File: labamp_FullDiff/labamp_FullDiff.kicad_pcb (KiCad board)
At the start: 2 copper layers, 55 x 26 mm, 33 parts, among them J1 Conn_02x06_Odd_Even, J2 Conn_02x06_Odd_Even, J3 Conn_01x03, U3 THS4521ID

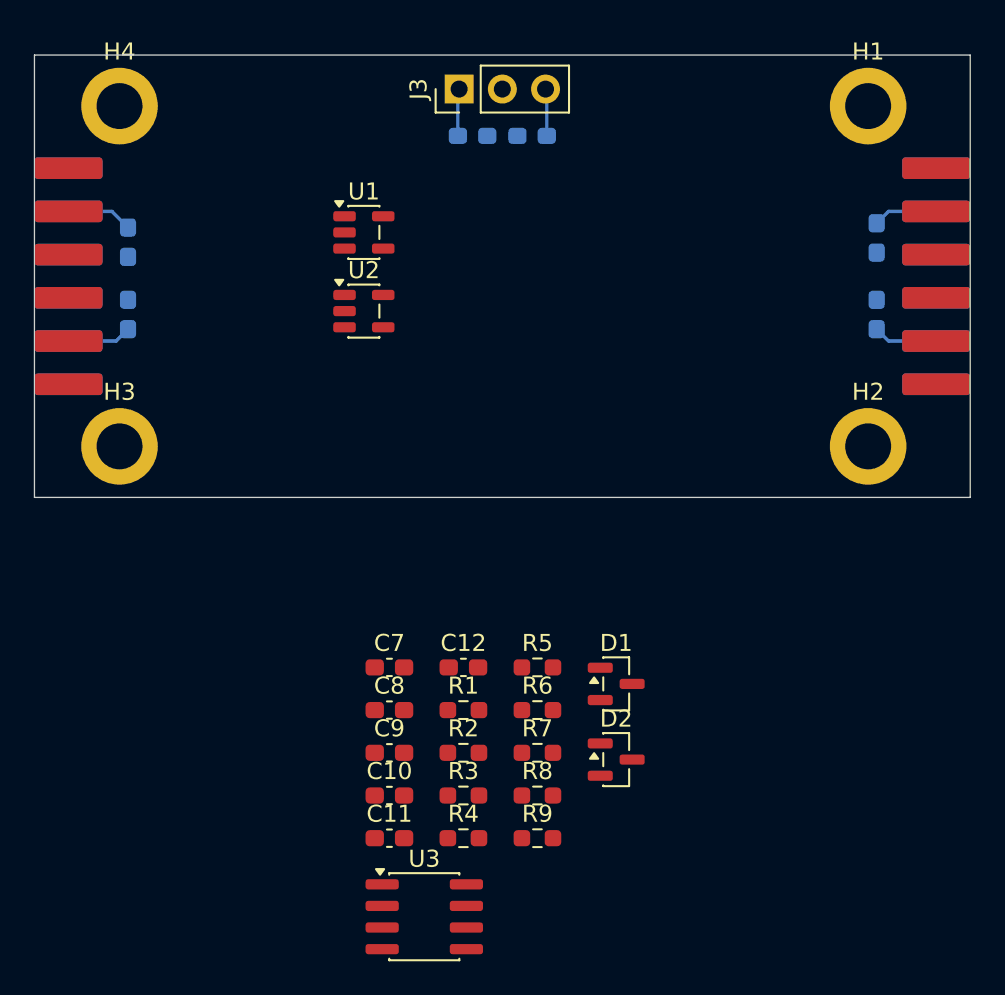
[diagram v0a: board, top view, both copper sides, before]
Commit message: PCB layout od Diff ampl started
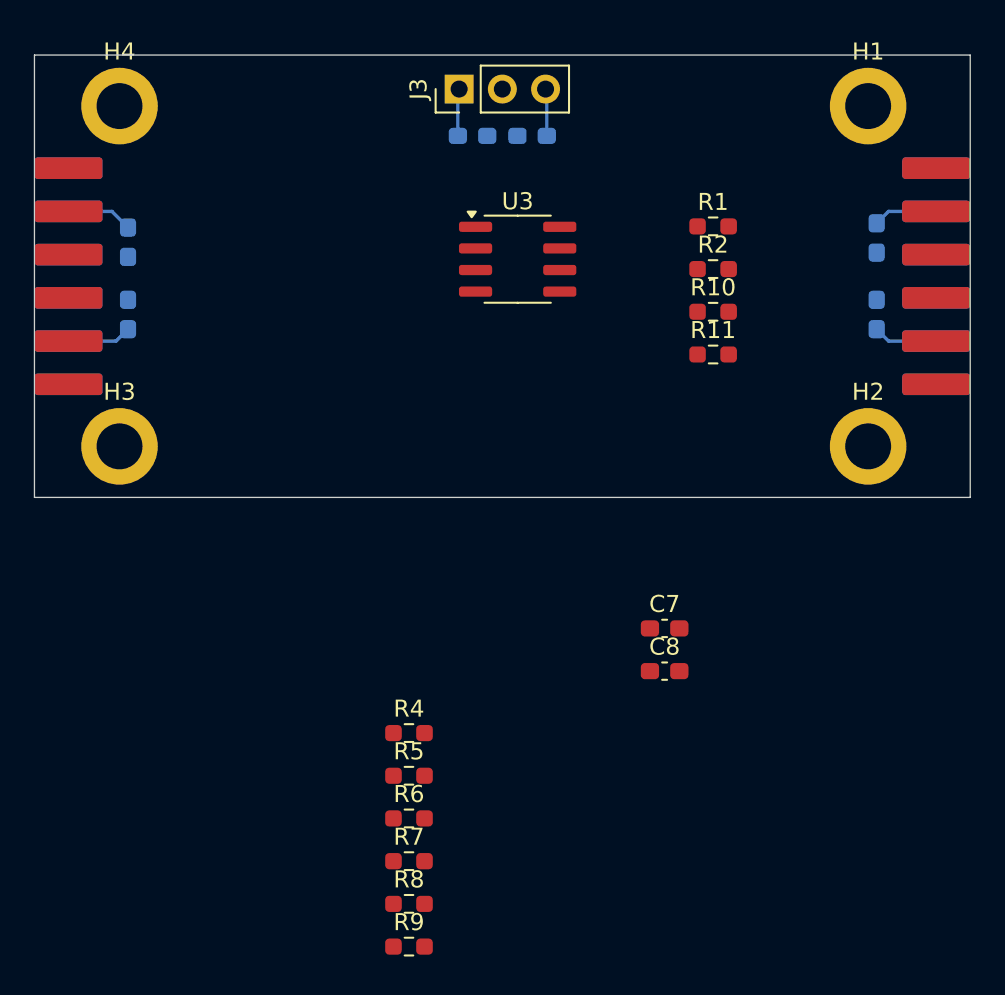
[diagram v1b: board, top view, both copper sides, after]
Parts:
- removed C10, C11, C12, C9: 100nF, Capacitor_SMD:C_0603_1608Metric_Pad1.08x0.95mm_HandSolder
- removed D1, D2: BAT54S, Package_TO_SOT_SMD:SOT-23
- removed R3: R, Resistor_SMD:R_0603_1608Metric_Pad0.98x0.95mm_HandSolder
- removed U1, U2: ~, Package_TO_SOT_SMD:SOT-23-5
- added R10: R, Resistor_SMD:R_0603_1608Metric_Pad0.98x0.95mm_HandSolder, F.Cu at (134.9, 92.1)
- added R11: R, Resistor_SMD:R_0603_1608Metric_Pad0.98x0.95mm_HandSolder, F.Cu at (134.9, 94.6)
- moved U3 39.0 mm to (123.4, 89.0)
- moved R1 32.0 mm to (134.9, 87.1)
- moved R2 32.0 mm to (134.9, 89.6)
- moved C7 16.3 mm to (132.0, 110.7)
- moved C8 16.3 mm to (132.0, 113.2)
- moved R5 9.88 mm to (117.0, 119.4)
- moved R6 9.88 mm to (117.0, 121.9)
- moved R8 9.88 mm to (117.0, 126.9)
- moved R9 9.88 mm to (117.0, 129.4)
- moved R7 9.88 mm to (117.0, 124.4)
- moved R4 6.96 mm to (117.0, 116.8)
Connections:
- R1 pad 1: Net-(U1--) -> GND
- R1 pad 2: Net-(U2--) -> Net-(R1-Pad2)
- R2 pad 1: Net-(R2-Pad1) -> GND
- R2 pad 2: Net-(U1--) -> Net-(R2-Pad2)
- R4 pad 2: /out- -> Net-(R10-Pad1)
- R5 pad 1: Net-(R2-Pad1) -> Net-(R2-Pad2)
- R6 pad 1: Net-(R3-Pad2) -> Net-(R1-Pad2)
- R7 pad 2: /out+ -> Net-(R11-Pad1)
- R8 pad 2: Net-(D1-COM) -> Net-(R2-Pad2)
- R9 pad 2: Net-(D2-COM) -> Net-(R1-Pad2)
- U3 pad 4: /out+ -> Net-(R11-Pad1)
- U3 pad 5: /out- -> Net-(R10-Pad1)

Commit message: Added option for single supply
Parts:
- added R12: R, Resistor_SMD:R_0603_1608Metric_Pad0.98x0.95mm_HandSolder, F.Cu at (125.5, 110.7)
- added R3: R, Resistor_SMD:R_0603_1608Metric_Pad0.98x0.95mm_HandSolder, F.Cu at (125.5, 108.2)
- moved C8 20.8 mm to (122.2, 94.9), turned to -90 degrees
- moved R6 11.0 mm to (128.0, 122.2)
- moved R7 8.05 mm to (123.6, 119.8)
- moved R8 6.03 mm to (122.4, 124.2)
- moved R9 5.37 mm to (122.2, 128.0)
- moved R1 4.78 mm to (132.2, 83.2)
- moved R2 4.10 mm to (137.6, 86.5)
- moved R10 2.54 mm to (136.8, 90.4)
- moved R5 2.42 mm to (116.6, 121.8)
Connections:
- U3 pad 2: GND -> Net-(U3-V_{OCM})
- U3 pad 3: unconnected-(U3-V_{S+}-Pad3) -> +3.3V
- U3 pad 6: unconnected-(U3-V_{S-}-Pad6) -> -3V3

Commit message: Updated template PCB layout rules
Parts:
- added C9: 100nF, Capacitor_SMD:C_0603_1608Metric_Pad1.08x0.95mm_HandSolder, F.Cu at (116.5, 90.8)
- moved R8 42.5 mm to (103.6, 86.2)
- moved R9 38.9 mm to (103.6, 93.8)
- moved R5 36.2 mm to (109.6, 86.2)
- moved R6 33.8 mm to (109.6, 93.8)
- moved R4 32.0 mm to (122.2, 85.3)
- moved R2 31.0 mm to (106.6, 88.2), turned to 90 degrees
- moved R1 27.0 mm to (106.6, 91.8), turned to -90 degrees
- moved R7 25.0 mm to (122.2, 94.8)
- moved R12 24.2 mm to (118.0, 87.7), turned to 90 degrees
- moved R3 23.0 mm to (115.2, 87.7), turned to -90 degrees
- moved C7 20.6 mm to (126.8, 90.8)
- moved C8 7.31 mm to (126.8, 89.2), turned to 0 degrees
- moved R11 5.84 mm to (134.2, 88.8), turned to 90 degrees
- moved R10 1.88 mm to (135.8, 88.8), turned to -90 degrees
- moved U3 1.64 mm to (122.2, 90.1), turned to 90 degrees
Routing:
- net +3.3V: track 10.6 -> 77.3 mm, vias 0 -> 1
- net Net-(R10-Pad1): track 0.00 -> 16.5 mm
- net /out+: track 0.00 -> 16.4 mm, vias 0 -> 2
- net Net-(R11-Pad1): track 0.00 -> 15.8 mm
- net /out-: track 0.00 -> 13.9 mm
- net Net-(U3-+): track 0.00 -> 13.9 mm
- net Net-(U3--): track 0.00 -> 12.4 mm
- net -3V3: track 10.6 -> 22.8 mm, vias 0 -> 1
- net Net-(U3-V_{OCM}): track 0.00 -> 10.3 mm
- net /in-: track 0.00 -> 5.69 mm
- net /in+: track 0.00 -> 5.69 mm
- net Net-(R2-Pad2): track 0.00 -> 5.08 mm
- net Net-(R1-Pad2): track 0.00 -> 5.08 mm

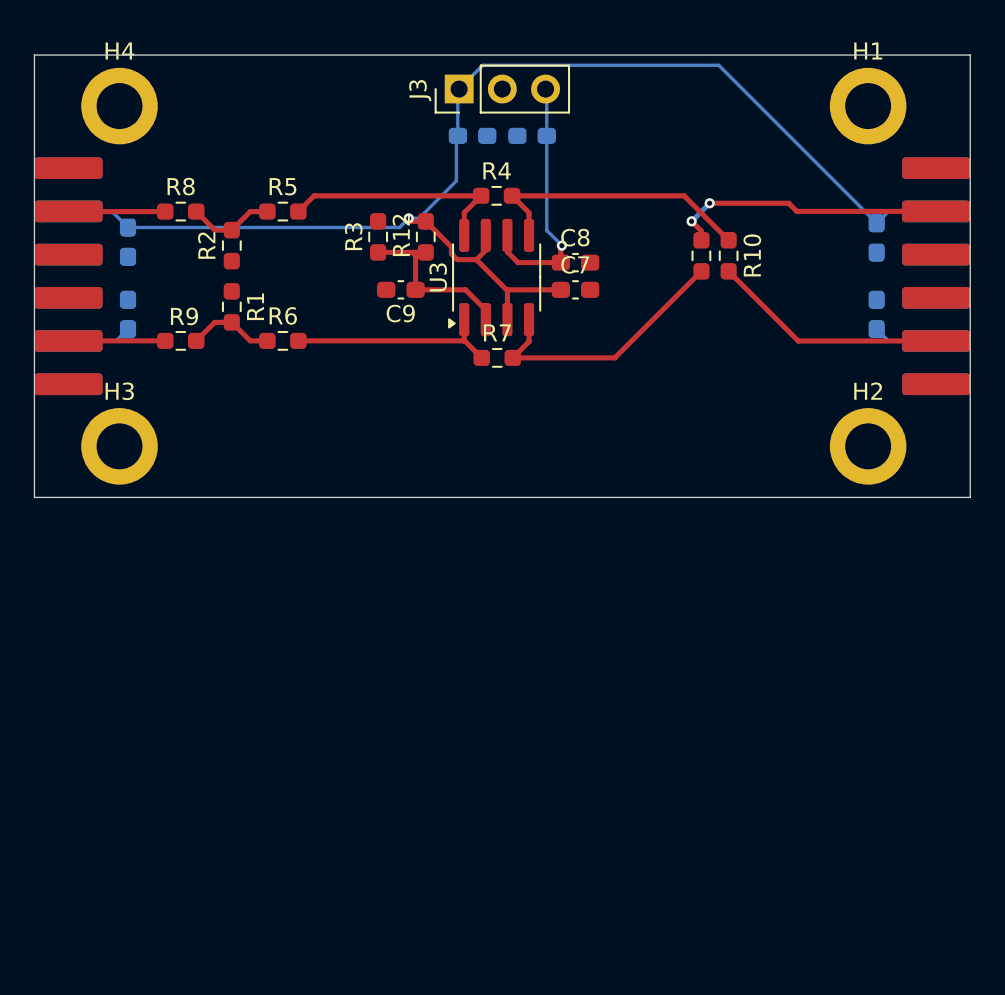
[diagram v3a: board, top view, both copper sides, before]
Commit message: Added pullup resistors on inputs
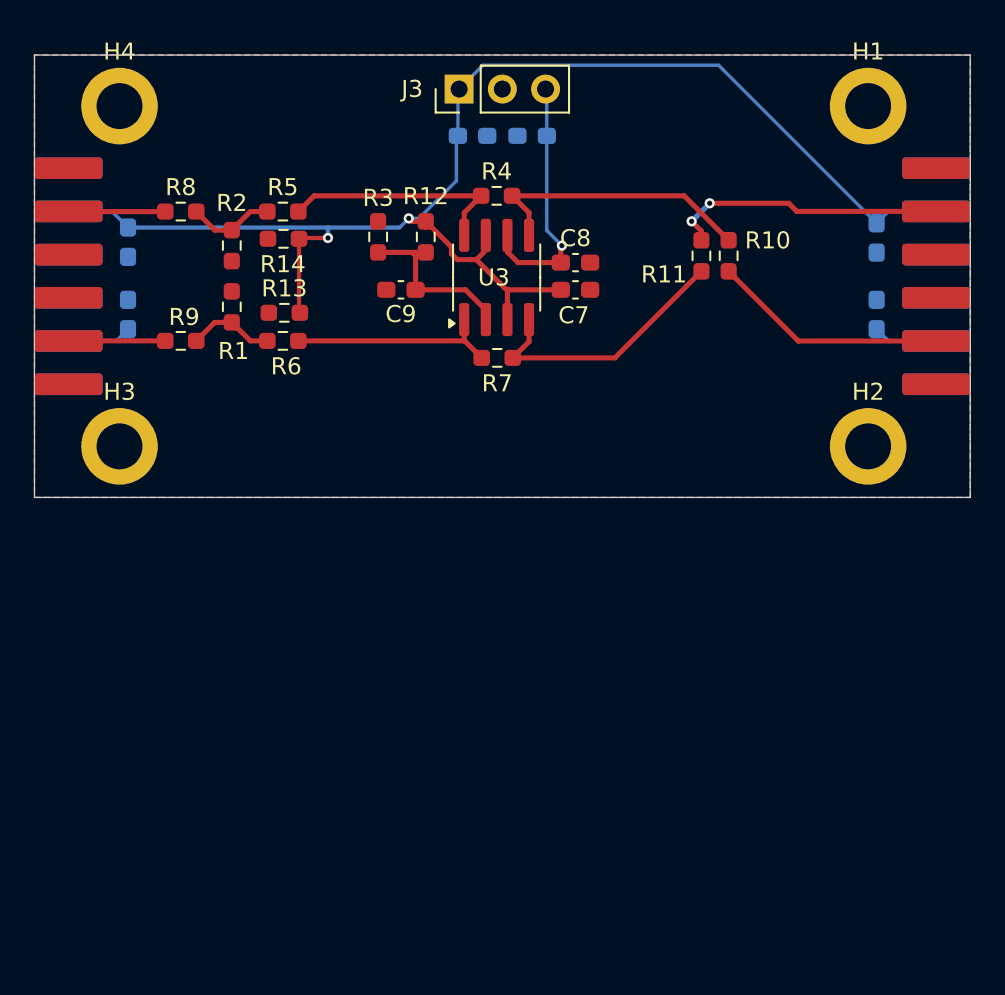
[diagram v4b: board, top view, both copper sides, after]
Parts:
- added R13: R, Resistor_SMD:R_0603_1608Metric_Pad0.98x0.95mm_HandSolder, F.Cu at (109.7, 92.2)
- added R14: R, Resistor_SMD:R_0603_1608Metric_Pad0.98x0.95mm_HandSolder, F.Cu at (109.6, 87.8)
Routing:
- net +3.3V: track 77.3 -> 84.0 mm, vias 1 -> 2
- added copper zone on B.Cu, net GND
- added copper zone on F.Cu, net GND

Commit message: Moved mounting holes to avoid colision with header
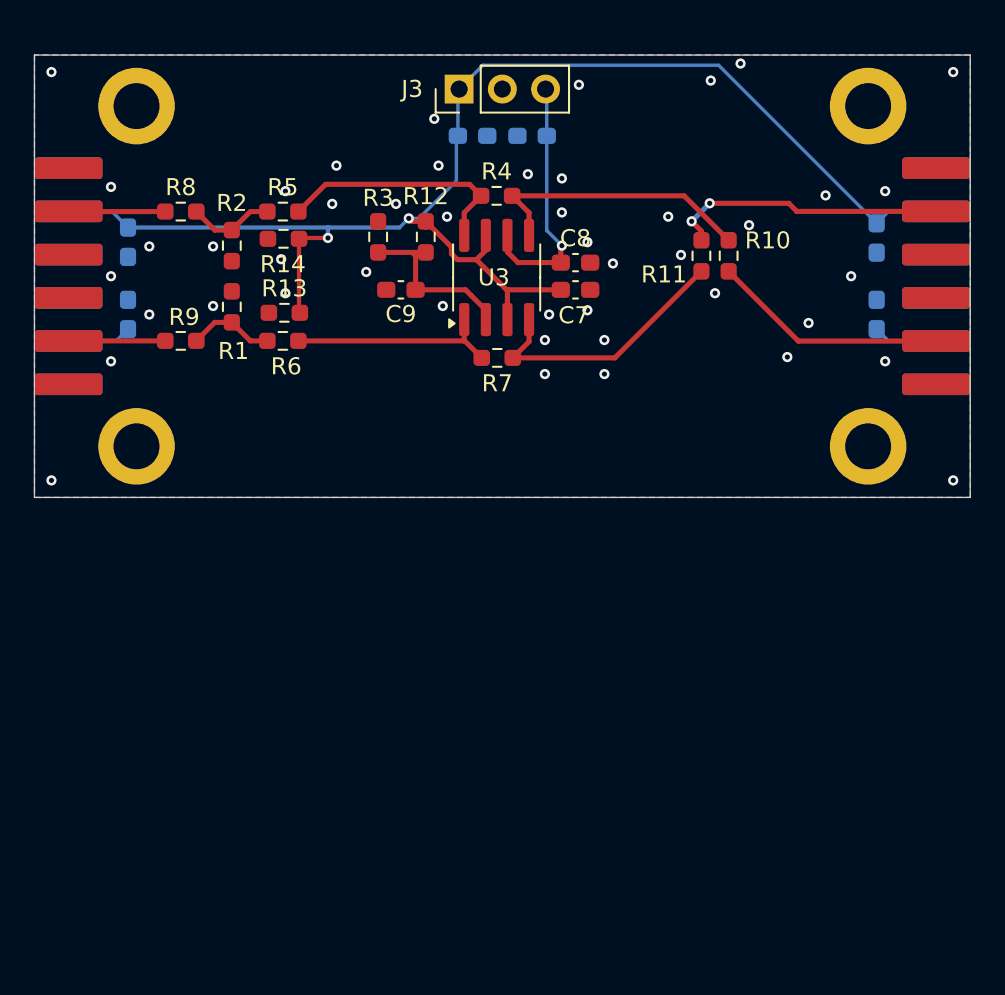
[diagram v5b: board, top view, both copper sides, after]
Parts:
- moved H3 1.00 mm to (101.0, 100.0)
- moved H4 1.00 mm to (101.0, 80.0)
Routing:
- net Net-(U3-+): track 13.9 -> 14.4 mm
- net GND: vias 0 -> 46

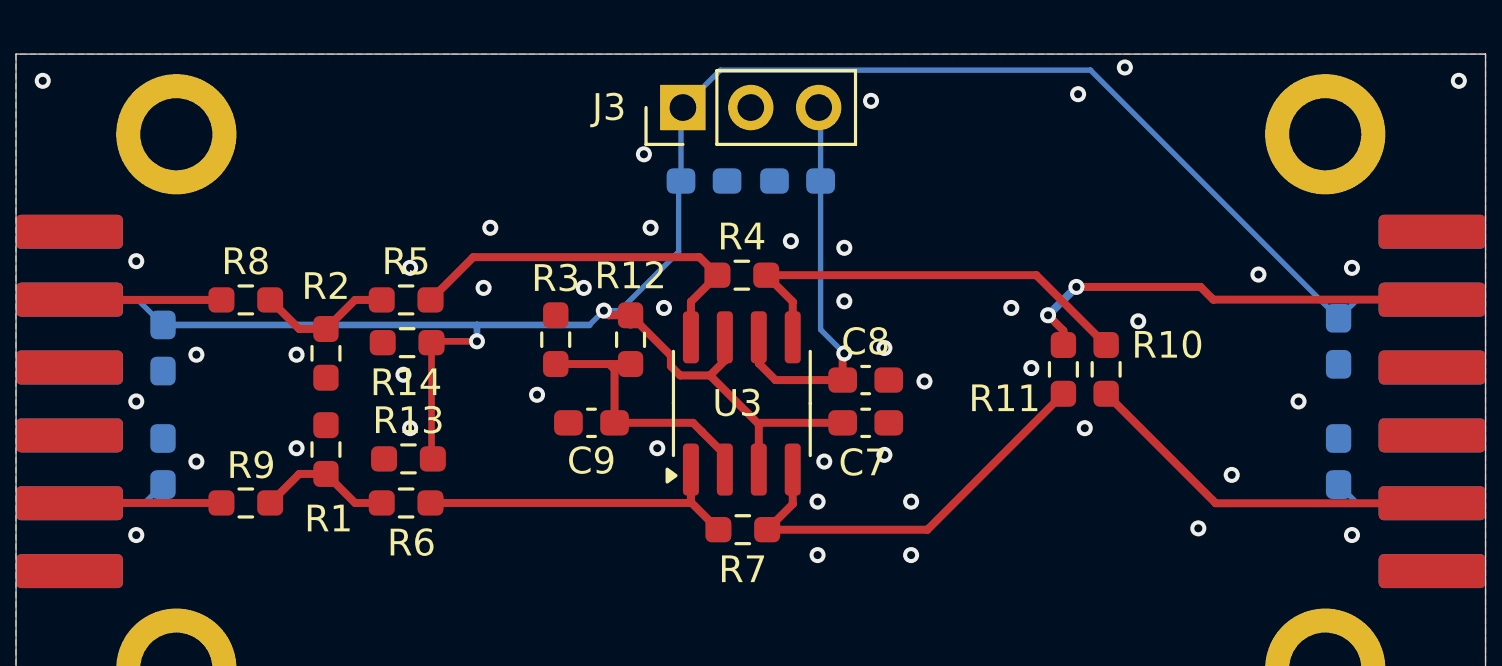
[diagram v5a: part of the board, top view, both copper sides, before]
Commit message: Finished FullDiff routing. PCB rules updated
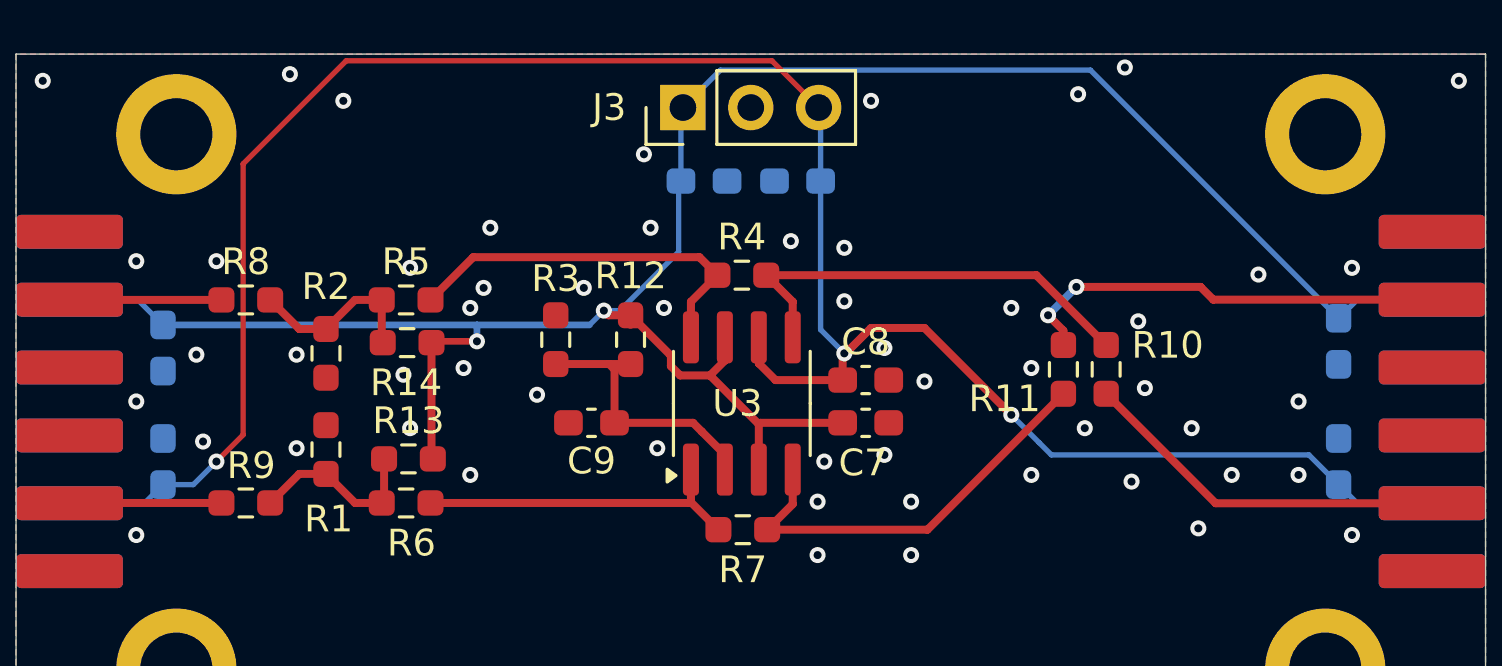
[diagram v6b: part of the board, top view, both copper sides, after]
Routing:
- net -3V3: track 22.8 -> 81.9 mm, vias 1 -> 3
- net Net-(R1-Pad2): track 5.08 -> 6.76 mm
- net Net-(R14-Pad1): track 5.08 -> 6.69 mm
- net GND: vias 46 -> 57

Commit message: Addedversion etc. in silkscreen
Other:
- board text added: "Full Diff Ver 1.0 BHH"
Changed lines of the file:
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@@
 		(layer "Edge.Cuts")
+	)
+	(gr_text "Full Diff\nVer 1.0\nBHH"
+		(at 133.1 84.5 0)
+		(layer "F.SilkS")
+		(effects
+			(font
+				(size 1.5 1.5)
+				(thickness 0.3)
+				(bold yes)
+			)
+			(justify bottom)
+		)
 	)
 	(via
